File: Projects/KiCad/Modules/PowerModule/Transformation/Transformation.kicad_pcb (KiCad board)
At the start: 2 copper layers, 110 x 95 mm, 50 parts, among them J1 Conn_01x02_Pin, J2 Conn_01x02_Pin, J3 Conn_01x02_Pin, J4 Conn_01x02_Pin, Q1 TJ8S06M3L, Q2 TJ8S06M3L, Q3 TJ8S06M3L, SW1 SW_SPDT, U1 NJM7812SDL1, U2 NJM7812SDL1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

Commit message: コネクタ位置を揃えた
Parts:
- J2: value Conn_01x02_Pin -> Conn_01x08; footprint Hirose_Connector:Hirose_DF1B -> Hirose_Connector:Hirose_DF11B-8DP-2DS
- moved J4 40.6 mm to (124.8, 128.4)
- moved J2 15.3 mm to (159.1, 128.9)
- moved J1 6.41 mm to (138.2, 128.4)
- moved J3 6.03 mm to (150.3, 128.4)
- moved C15 5.30 mm to (118.8, 119.1)
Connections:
- J2 pad 1: GND -> +12V
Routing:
- net Net-(J4-Pin_2): track 34.8 -> 83.4 mm
- net +12V: track 23.6 -> 40.8 mm
- net +BATT: track 100.0 -> 94.8 mm
- net +VDC: track 49.7 -> 52.7 mm
- net Net-(J2-Pin_7): track 0.00 -> 2.00 mm
- net Net-(J2-Pin_3): track 0.00 -> 2.00 mm
- net +VSW: track 24.5 -> 23.0 mm
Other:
- board text added: "BATT VREF POOL"
- board text removed: "BATT VREF VSW"
- board text removed: "INTERNAL 12V"

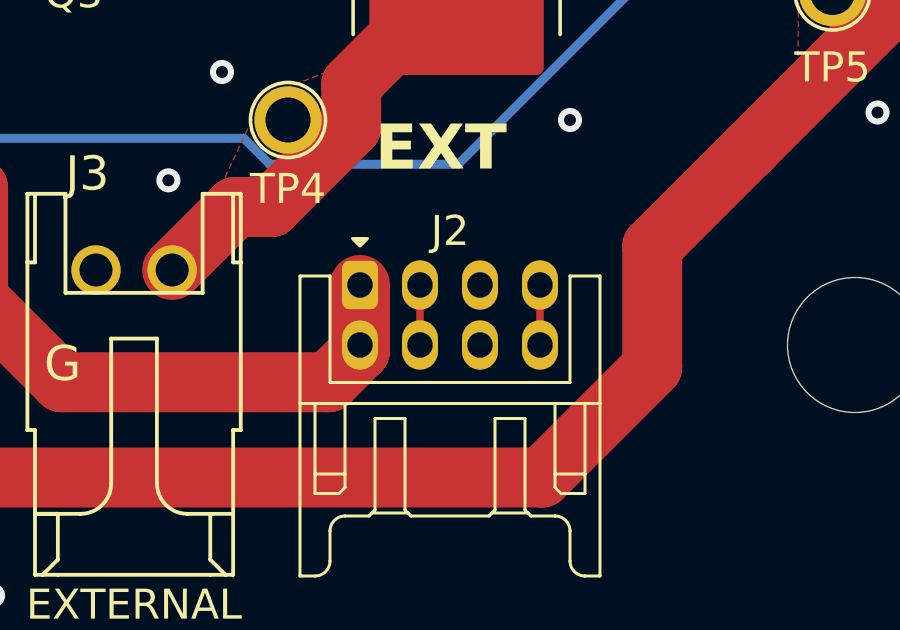
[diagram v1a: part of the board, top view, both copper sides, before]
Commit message: コネクタのピン配置を変更
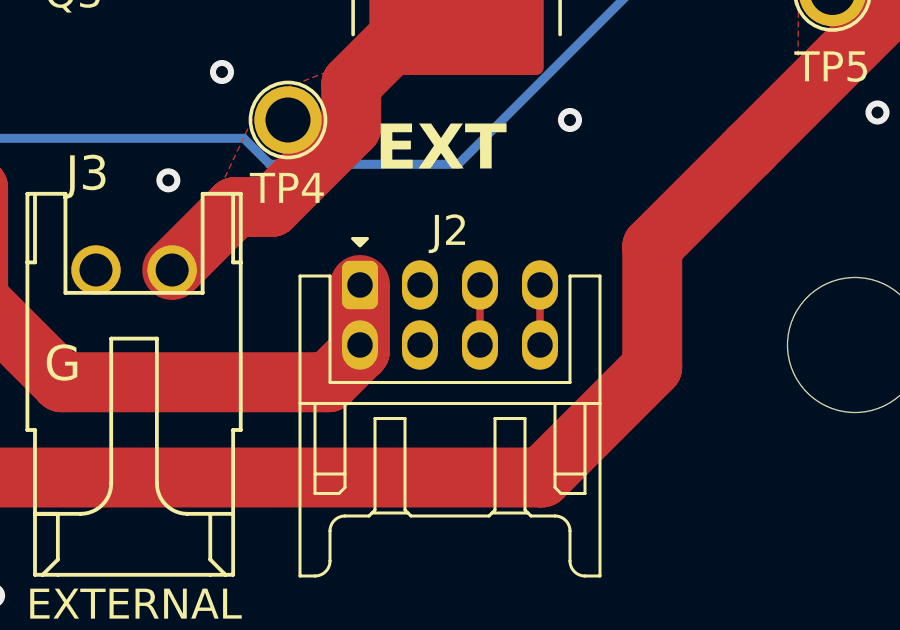
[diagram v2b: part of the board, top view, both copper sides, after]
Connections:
- J2 pad 3: Net-(J2-Pin_3) -> GND
- J2 pad 4: Net-(J2-Pin_3) -> GND
- J2 pad 5: GND -> Net-(J2-Pin_5)
- J2 pad 6: GND -> Net-(J2-Pin_5)
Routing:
- net Net-(J2-Pin_5): track 0.00 -> 2.00 mm
- net Net-(J2-Pin_3): track 2.00 -> 0.00 mm

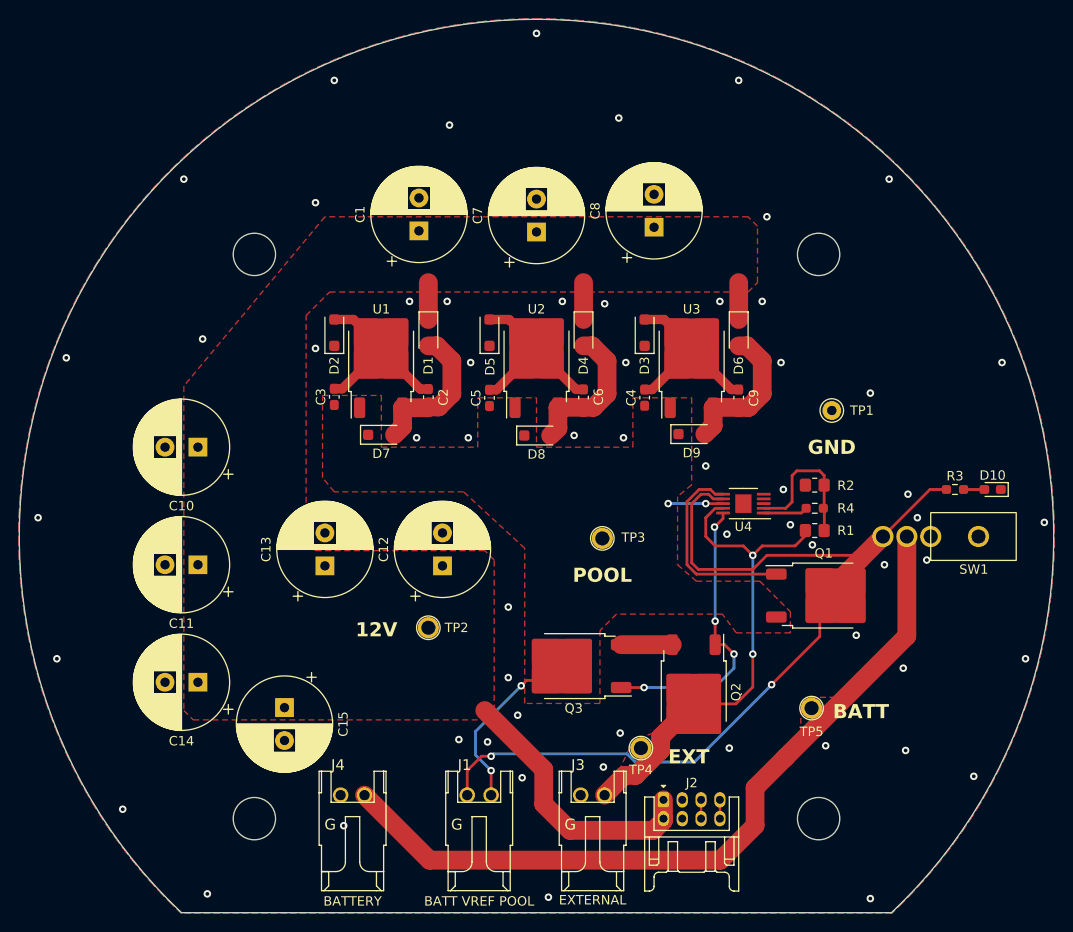
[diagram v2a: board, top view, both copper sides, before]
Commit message: バッファコンデンサを表面実装に変更
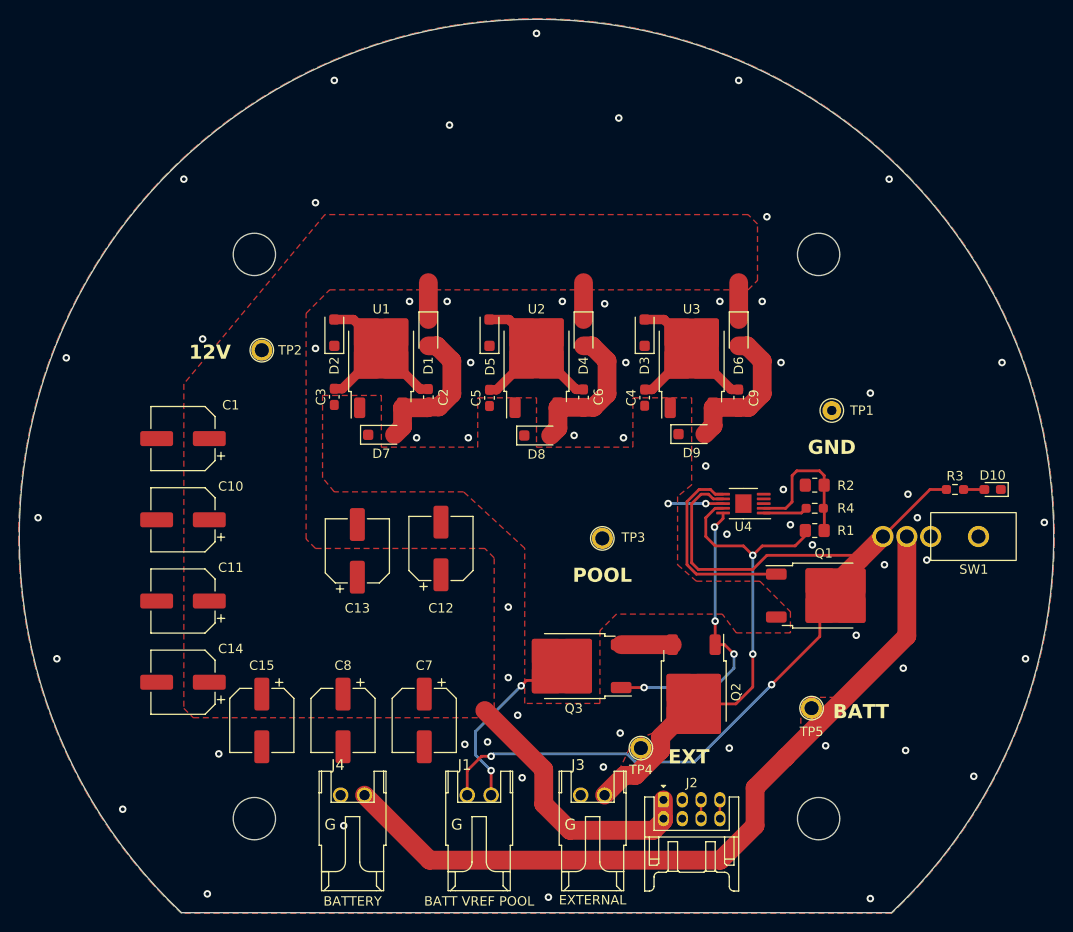
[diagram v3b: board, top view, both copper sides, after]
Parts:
- C1, C10, C11, C12, C13, C14, C15, C7, C8: value 270μF -> 100μF; footprint Capacitor_THT:CP_Radial_D10.0mm_P3.50mm -> Capacitor_SMD:CP_Elec_6.3x5.9
- moved C8 62.0 mm to (125.0, 120.5), turned to -90 degrees
- moved C7 53.3 mm to (133.7, 120.5), turned to -90 degrees
- moved TP2 34.4 mm to (116.4, 81.1)
- moved C1 33.4 mm to (108.0, 90.5), turned to 180 degrees
- moved C10 7.88 mm to (108.0, 99.2)
- moved C11 4.17 mm to (108.0, 107.8)
- moved C13 3.80 mm to (126.6, 102.5)
- moved C15 2.77 mm to (116.4, 120.5)
- moved C12 1.85 mm to (135.4, 102.2)
- moved C14 1.59 mm to (108.0, 116.4)

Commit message: チェックよし（多分）
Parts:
- U4: footprint Package_SO:MSOP-10-1EP_3x3mm_P0.5mm_EP1.73x1.98mm -> Package_SO:MSOP-10-1EP_3x3mm_P0.5mm_EP1.68x1.88mm
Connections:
- U4 pad 11: (no net) -> GND
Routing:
- net GND: track 0.00 -> 7.92 mm
- net Net-(U4-E1): track 15.7 -> 12.3 mm
- net Net-(J4-Pin_2): track 83.4 -> 85.1 mm
